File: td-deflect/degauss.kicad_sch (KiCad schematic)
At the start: 10 parts

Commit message: more updates
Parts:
- R108, R109: renamed from R?; footprint (none) -> Resistor_SMD:R_0805_2012Metric_Pad1.15x1.40mm_HandSolder
- gave numbers to parts that had none: 8
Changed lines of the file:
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@@
   (symbol (lib_id "Connector:Conn_01x02_Male") (at 181.61 95.25 0) (mirror y) (unit 1)
     (in_bom yes) (on_board yes) (dnp no)
-    (property "Reference" "J?" (at 178.8668 90.6526 0)
+    (property "Reference" "J15" (at 178.8668 90.6526 0)
       (effects (font (size 1.27 1.27)))
     )
@@
       (project "td-deflect"
         (path "/55a1a5e1-4d11-4c3e-b2b4-b9d50ddc5f9d/76858b88-020a-4ca7-9465-04c6cdf1756c"
-          (reference "J?") (unit 1)
+          (reference "J15") (unit 1)
         )
       )
@@
   (symbol (lib_id "Driver_FET:MCP1416") (at 128.27 83.82 0) (unit 1)
     (in_bom yes) (on_board yes) (dnp no)
-    (property "Reference" "U?" (at 139.5476 82.6516 0)
+    (property "Reference" "U38" (at 139.5476 82.6516 0)
       (effects (font (size 1.27 1.27)) (justify left))
     )
@@
       (project "td-deflect"
         (path "/55a1a5e1-4d11-4c3e-b2b4-b9d50ddc5f9d/76858b88-020a-4ca7-9465-04c6cdf1756c"
-          (reference "U?") (unit 1)
+          (reference "U38") (unit 1)
         )
       )
@@
   (symbol (lib_id "power:+12V") (at 96.52 81.28 0) (unit 1)
     (in_bom yes) (on_board yes) (dnp no)
-    (property "Reference" "#PWR?" (at 96.52 85.09 0)
+    (property "Reference" "#PWR0218" (at 96.52 85.09 0)
       (effects (font (size 1.27 1.27)) hide)
     )
@@
       (project "td-deflect"
         (path "/55a1a5e1-4d11-4c3e-b2b4-b9d50ddc5f9d/76858b88-020a-4ca7-9465-04c6cdf1756c"
-          (reference "#PWR?") (unit 1)
+          (reference "#PWR0218") (unit 1)
         )
       )
@@
   (symbol (lib_id "Transistor_FET:IPD50R380CE") (at 151.13 83.82 0) (unit 1)
     (in_bom yes) (on_board yes) (dnp no)
-    (property "Reference" "Q?" (at 147.32 87.63 0)
+    (property "Reference" "Q22" (at 147.32 87.63 0)
       (effects (font (size 1.27 1.27)) (justify left))
     )
@@
       (project "td-deflect"
         (path "/55a1a5e1-4d11-4c3e-b2b4-b9d50ddc5f9d/76858b88-020a-4ca7-9465-04c6cdf1756c"
-          (reference "Q?") (unit 1)
+          (reference "Q22") (unit 1)
         )
       )
@@
   (symbol (lib_id "power:GND") (at 168.91 88.9 0) (unit 1)
     (in_bom yes) (on_board yes) (dnp no) (fields_autoplaced)
-    (property "Reference" "#PWR?" (at 168.91 95.25 0)
+    (property "Reference" "#PWR0214" (at 168.91 95.25 0)
       (effects (font (size 1.27 1.27)) hide)
     )
@@
       (project "td-deflect"
         (path "/55a1a5e1-4d11-4c3e-b2b4-b9d50ddc5f9d/76858b88-020a-4ca7-9465-04c6cdf1756c"
-          (reference "#PWR?") (unit 1)
+          (reference "#PWR0214") (unit 1)
         )
       )
@@
   (symbol (lib_id "Device:C") (at 96.52 85.09 0) (unit 1)
     (in_bom yes) (on_board yes) (dnp no)
-    (property "Reference" "C?" (at 99.441 83.9216 0)
+    (property "Reference" "C88" (at 99.441 83.9216 0)
       (effects (font (size 1.27 1.27)) (justify left))
     )
@@
       (project "td-deflect"
         (path "/55a1a5e1-4d11-4c3e-b2b4-b9d50ddc5f9d/76858b88-020a-4ca7-9465-04c6cdf1756c"
-          (reference "C?") (unit 1)
+          (reference "C88") (unit 1)
         )
       )
@@
   (symbol (lib_id "power:GND") (at 128.27 91.44 0) (unit 1)
     (in_bom yes) (on_board yes) (dnp no) (fields_autoplaced)
-    (property "Reference" "#PWR?" (at 128.27 97.79 0)
+    (property "Reference" "#PWR0216" (at 128.27 97.79 0)
       (effects (font (size 1.27 1.27)) hide)
     )
@@
       (project "td-deflect"
         (path "/55a1a5e1-4d11-4c3e-b2b4-b9d50ddc5f9d/76858b88-020a-4ca7-9465-04c6cdf1756c"
-          (reference "#PWR?") (unit 1)
+          (reference "#PWR0216") (unit 1)
         )
       )
@@
   (symbol (lib_id "power:+12V") (at 128.27 76.2 0) (unit 1)
     (in_bom yes) (on_board yes) (dnp no) (fields_autoplaced)
-    (property "Reference" "#PWR?" (at 128.27 80.01 0)
+    (property "Reference" "#PWR0217" (at 128.27 80.01 0)
       (effects (font (size 1.27 1.27)) hide)
     )
@@
       (project "td-deflect"
         (path "/55a1a5e1-4d11-4c3e-b2b4-b9d50ddc5f9d/76858b88-020a-4ca7-9465-04c6cdf1756c"
-          (reference "#PWR?") (unit 1)
+          (reference "#PWR0217") (unit 1)
         )
       )
@@
   (symbol (lib_id "power:GND") (at 96.52 88.9 0) (unit 1)
     (in_bom yes) (on_board yes) (dnp no)
-    (property "Reference" "#PWR?" (at 96.52 95.25 0)
+    (property "Reference" "#PWR0219" (at 96.52 95.25 0)
       (effects (font (size 1.27 1.27)) hide)
     )
@@
       (project "td-deflect"
         (path "/55a1a5e1-4d11-4c3e-b2b4-b9d50ddc5f9d/76858b88-020a-4ca7-9465-04c6cdf1756c"
-          (reference "#PWR?") (unit 1)
+          (reference "#PWR0219") (unit 1)
         )
       )
@@
   (symbol (lib_id "power:HT") (at 168.91 57.15 0) (unit 1)
     (in_bom yes) (on_board yes) (dnp no) (fields_autoplaced)
-    (property "Reference" "#PWR?" (at 168.91 54.102 0)
+    (property "Reference" "#PWR0213" (at 168.91 54.102 0)
       (effects (font (size 1.27 1.27)) hide)
     )
@@
       (project "td-deflect"
         (path "/55a1a5e1-4d11-4c3e-b2b4-b9d50ddc5f9d/76858b88-020a-4ca7-9465-04c6cdf1756c"
-          (reference "#PWR?") (unit 1)
+          (reference "#PWR0213") (unit 1)
         )
       )
@@
   (symbol (lib_id "Diode:BA157") (at 168.91 62.23 90) (unit 1)
     (in_bom yes) (on_board yes) (dnp no)
-    (property "Reference" "D?" (at 174.3964 62.23 0)
+    (property "Reference" "D20" (at 174.3964 62.23 0)
       (effects (font (size 1.27 1.27)))
     )
@@
       (project "td-deflect"
         (path "/55a1a5e1-4d11-4c3e-b2b4-b9d50ddc5f9d/76858b88-020a-4ca7-9465-04c6cdf1756c"
-          (reference "D?") (unit 1)
+          (reference "D20") (unit 1)
         )
       )
@@
   (symbol (lib_id "Device:R") (at 116.84 87.63 0) (unit 1)
     (in_bom yes) (on_board yes) (dnp no) (fields_autoplaced)
-    (property "Reference" "R?" (at 119.38 86.3599 0)
+    (property "Reference" "R108" (at 119.38 86.3599 0)
       (effects (font (size 1.27 1.27)) (justify left))
     )
@@
       (effects (font (size 1.27 1.27)) (justify left))
     )
-    (property "Footprint" "" (at 115.062 87.63 90)
+    (property "Footprint" "Resistor_SMD:R_0805_2012Metric_Pad1.15x1.40mm_HandSolder" (at 115.062 87.63 90)
       (effects (font (size 1.27 1.27)) hide)
     )
@@
       (project "td-deflect"
         (path "/55a1a5e1-4d11-4c3e-b2b4-b9d50ddc5f9d/76858b88-020a-4ca7-9465-04c6cdf1756c"
-          (reference "R?") (unit 1)
+          (reference "R108") (unit 1)
         )
       )
@@
   (symbol (lib_id "Device:R") (at 168.91 69.85 0) (unit 1)
     (in_bom yes) (on_board yes) (dnp no) (fields_autoplaced)
-    (property "Reference" "R?" (at 171.45 68.5799 0)
+    (property "Reference" "R110" (at 171.45 68.5799 0)
       (effects (font (size 1.27 1.27)) (justify left))
     )
@@
       (project "td-deflect"
         (path "/55a1a5e1-4d11-4c3e-b2b4-b9d50ddc5f9d/76858b88-020a-4ca7-9465-04c6cdf1756c"
-          (reference "R?") (unit 1)
+          (reference "R110") (unit 1)
         )
       )
@@
   (symbol (lib_id "Device:C") (at 168.91 77.47 0) (unit 1)
     (in_bom yes) (on_board yes) (dnp no)
-    (property "Reference" "C?" (at 171.831 76.3016 0)
+    (property "Reference" "C89" (at 171.831 76.3016 0)
       (effects (font (size 1.27 1.27)) (justify left))
     )
@@
       (project "td-deflect"
         (path "/55a1a5e1-4d11-4c3e-b2b4-b9d50ddc5f9d/76858b88-020a-4ca7-9465-04c6cdf1756c"
-          (reference "C?") (unit 1)
+          (reference "C89") (unit 1)
         )
       )
@@
   (symbol (lib_id "Connector:Conn_01x02_Male") (at 176.53 82.55 0) (mirror y) (unit 1)
     (in_bom yes) (on_board yes) (dnp no)
-    (property "Reference" "J?" (at 173.7868 77.9526 0)
+    (property "Reference" "J12" (at 173.7868 77.9526 0)
       (effects (font (size 1.27 1.27)))
     )
@@
       (project "td-deflect"
         (path "/55a1a5e1-4d11-4c3e-b2b4-b9d50ddc5f9d/76858b88-020a-4ca7-9465-04c6cdf1756c"
-          (reference "J?") (unit 1)
+          (reference "J12") (unit 1)
         )
       )
@@
   (symbol (lib_id "power:GND") (at 116.84 91.44 0) (unit 1)
     (in_bom yes) (on_board yes) (dnp no) (fields_autoplaced)
-    (property "Reference" "#PWR?" (at 116.84 97.79 0)
+    (property "Reference" "#PWR0215" (at 116.84 97.79 0)
       (effects (font (size 1.27 1.27)) hide)
     )
@@
       (project "td-deflect"
         (path "/55a1a5e1-4d11-4c3e-b2b4-b9d50ddc5f9d/76858b88-020a-4ca7-9465-04c6cdf1756c"
-          (reference "#PWR?") (unit 1)
+          (reference "#PWR0215") (unit 1)
         )
       )
@@
   (symbol (lib_id "Device:R") (at 142.24 83.82 90) (unit 1)
     (in_bom yes) (on_board yes) (dnp no) (fields_autoplaced)
-    (property "Reference" "R?" (at 142.24 77.47 90)
+    (property "Reference" "R109" (at 142.24 77.47 90)
       (effects (font (size 1.27 1.27)))
     )
@@
       (effects (font (size 1.27 1.27)))
     )
-    (property "Footprint" "" (at 142.24 85.598 90)
+    (property "Footprint" "Resistor_SMD:R_0805_2012Metric_Pad1.15x1.40mm_HandSolder" (at 142.24 85.598 90)
       (effects (font (size 1.27 1.27)) hide)
     )
@@
       (project "td-deflect"
         (path "/55a1a5e1-4d11-4c3e-b2b4-b9d50ddc5f9d/76858b88-020a-4ca7-9465-04c6cdf1756c"
-          (reference "R?") (unit 1)
-        )
-      )
+          (reference "R109") (unit 1)
+        )
+      )

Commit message: switch to new 0805 footprint
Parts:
- C88: footprint Capacitor_SMD:C_0805_2012Metric_Pad1.15x1.40mm_HandSolder -> Capacitor_SMD:C_0805_2012Metric_Pad1.18x1.45mm_HandSolder
- R108, R109: footprint Resistor_SMD:R_0805_2012Metric_Pad1.15x1.40mm_HandSolder -> Resistor_SMD:R_0805_2012Metric_Pad1.20x1.40mm_HandSolder
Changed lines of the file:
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@@
       (effects (font (size 1.27 1.27)) (justify left))
     )
-    (property "Footprint" "Capacitor_SMD:C_0805_2012Metric_Pad1.15x1.40mm_HandSolder" (at 97.4852 88.9 0)
+    (property "Footprint" "Capacitor_SMD:C_0805_2012Metric_Pad1.18x1.45mm_HandSolder" (at 97.4852 88.9 0)
       (effects (font (size 1.27 1.27)) hide)
     )
@@
       (effects (font (size 1.27 1.27)) (justify left))
     )
-    (property "Footprint" "Resistor_SMD:R_0805_2012Metric_Pad1.15x1.40mm_HandSolder" (at 115.062 87.63 90)
+    (property "Footprint" "Resistor_SMD:R_0805_2012Metric_Pad1.20x1.40mm_HandSolder" (at 115.062 87.63 90)
       (effects (font (size 1.27 1.27)) hide)
     )
@@
       (effects (font (size 1.27 1.27)))
     )
-    (property "Footprint" "Resistor_SMD:R_0805_2012Metric_Pad1.15x1.40mm_HandSolder" (at 142.24 85.598 90)
-      (effects (font (size 1.27 1.27)) hide)
-    )
+    (property "Footprint" "Resistor_SMD:R_0805_2012Metric_Pad1.20x1.40mm_HandSolder" (at 142.24 85.598 90)
+      (effects (font (size 1.27 1.27)) hide)
+    )

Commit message: fix drc errors
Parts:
- J12, J15: symbol Connector:Conn_01x02_Male -> Connector:Conn_01x02_Pin
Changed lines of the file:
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@@
     )
   )
-  (symbol (lib_id "Connector:Conn_01x02_Male") (at 181.61 95.25 0) (mirror y) (unit 1)
+  (symbol (lib_id "Connector:Conn_01x02_Pin") (at 181.61 95.25 0) (mirror y) (unit 1)
     (in_bom yes) (on_board yes) (dnp no)
     (property "Reference" "J15" (at 178.8668 90.6526 0)
@@
     )
   )
-  (symbol (lib_id "Connector:Conn_01x02_Male") (at 176.53 82.55 0) (mirror y) (unit 1)
+  (symbol (lib_id "Connector:Conn_01x02_Pin") (at 176.53 82.55 0) (mirror y) (unit 1)
     (in_bom yes) (on_board yes) (dnp no)
     (property "Reference" "J12" (at 173.7868 77.9526 0)

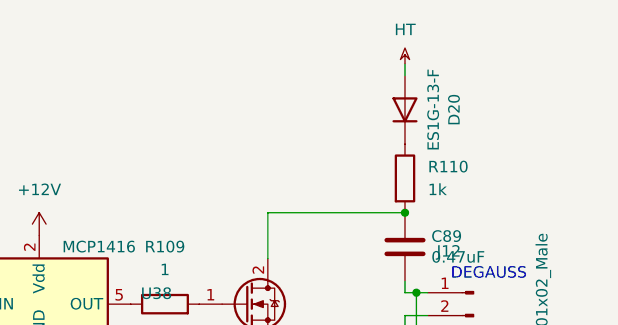
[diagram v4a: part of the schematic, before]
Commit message: fix remaining erc errors
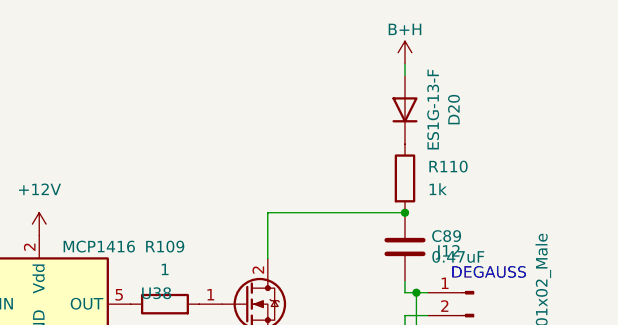
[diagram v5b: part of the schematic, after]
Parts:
- D20: footprint Diode_SMD:D_SMA -> Diode_THT:D_DO-41_SOD81_P10.16mm_Horizontal
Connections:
- net HT renamed B+H
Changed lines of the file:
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@@
+    )
+  )
+  (symbol (lib_id "td-crt:B+H") (at 168.91 57.15 0) (unit 1)
+    (in_bom yes) (on_board yes) (dnp no) (fields_autoplaced)
+    (property "Reference" "#PWR024" (at 168.91 60.96 0)
+      (effects (font (size 1.27 1.27)) hide)
+    )
+    (property "Value" "B+H" (at 168.91 53.34 0)
+      (effects (font (size 1.27 1.27)))
+    )
+    (property "Footprint" "" (at 168.91 57.15 0)
+      (effects (font (size 1.27 1.27)) hide)
+    )
+    (property "Datasheet" "" (at 168.91 57.15 0)
+      (effects (font (size 1.27 1.27)) hide)
+    )
+    (pin "1")
+    (instances
+      (project "td-deflect"
+        (path "/55a1a5e1-4d11-4c3e-b2b4-b9d50ddc5f9d/76858b88-020a-4ca7-9465-04c6cdf1756c"
+          (reference "#PWR024") (unit 1)
+        )
+      )
     )
   )
@@
     )
   )
-  (symbol (lib_id "power:HT") (at 168.91 57.15 0) (unit 1)
-    (in_bom yes) (on_board yes) (dnp no) (fields_autoplaced)
-    (property "Reference" "#PWR0213" (at 168.91 54.102 0)
-      (effects (font (size 1.27 1.27)) hide)
-    )
-    (property "Value" "HT" (at 168.91 53.34 0)
-      (effects (font (size 1.27 1.27)))
-    )
-    (property "Footprint" "" (at 168.91 57.15 0)
-      (effects (font (size 1.27 1.27)) hide)
-    )
-    (property "Datasheet" "" (at 168.91 57.15 0)
-      (effects (font (size 1.27 1.27)) hide)
-    )
-    (pin "1")
-    (instances
-      (project "td-deflect"
-        (path "/55a1a5e1-4d11-4c3e-b2b4-b9d50ddc5f9d/76858b88-020a-4ca7-9465-04c6cdf1756c"
-          (reference "#PWR0213") (unit 1)
-        )
-      )
-    )
-  )
   (symbol (lib_id "Diode:BA157") (at 168.91 62.23 90) (unit 1)
     (in_bom yes) (on_board yes) (dnp no)
@@
       (effects (font (size 1.27 1.27)))
     )
-    (property "Footprint" "Diode_SMD:D_SMA" (at 173.355 62.23 0)
-      (effects (font (size 1.27 1.27)) hide)
-    )
-    (property "Datasheet" "" (at 168.91 62.23 0)
-      (effects (font (size 1.27 1.27)) hide)
-    )
+    (property "Footprint" "Diode_THT:D_DO-41_SOD81_P10.16mm_Horizontal" (at 173.355 62.23 0)
+      (effects (font (size 1.27 1.27)) hide)
+    )
+    (property "Datasheet" "https://www.vishay.com/docs/88536/ba157.pdf" (at 168.91 62.23 0)
+      (effects (font (size 1.27 1.27)) hide)
+    )

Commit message: more layout work
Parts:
- removed J15: Conn_01x02_Male, td-deflect:monitor_10_8_2p, symbol Connector:Conn_01x02_Pin
- D20: footprint Diode_THT:D_DO-41_SOD81_P10.16mm_Horizontal -> Diode_SMD:D_SMA
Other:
- note removed: "DEGAUSS 2"
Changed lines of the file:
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@@
 (kicad_sch (version 20230121) (generator eeschema)
   (paper "A4")
-  (junction (at 170.18 82.55) (diameter 0) (color 0 0 0 0)
-  )
   (junction (at 116.84 83.82) (diameter 0) (color 0 0 0 0)
   )
@@
   (junction (at 168.91 73.66) (diameter 0) (color 0 0 0 0)
   )
-  (wire (pts (xy 170.18 87.63) (xy 176.53 87.63))
-    (stroke (width 0) (type default))
-  )
   (wire (pts (xy 168.91 85.09) (xy 168.91 88.9))
     (stroke (width 0) (type default))
   )
-  (wire (pts (xy 170.18 82.55) (xy 171.45 82.55))
-    (stroke (width 0) (type default))
-  )
   (wire (pts (xy 168.91 57.15) (xy 168.91 58.42))
     (stroke (width 0) (type default))
@@
     (stroke (width 0) (type default))
   )
-  (wire (pts (xy 171.45 97.79) (xy 176.53 97.79))
-    (stroke (width 0) (type default))
-  )
   (wire (pts (xy 168.91 81.28) (xy 168.91 82.55))
     (stroke (width 0) (type default))
   )
-  (wire (pts (xy 168.91 82.55) (xy 170.18 82.55))
+  (wire (pts (xy 168.91 82.55) (xy 171.45 82.55))
     (stroke (width 0) (type default))
   )
@@
     (stroke (width 0) (type default))
   )
-  (wire (pts (xy 171.45 88.9) (xy 171.45 97.79))
-    (stroke (width 0) (type default))
-  )
   (wire (pts (xy 171.45 85.09) (xy 168.91 85.09))
     (stroke (width 0) (type default))
   )
-  (wire (pts (xy 176.53 87.63) (xy 176.53 95.25))
-    (stroke (width 0) (type default))
-  )
-  (wire (pts (xy 170.18 82.55) (xy 170.18 87.63))
-    (stroke (width 0) (type default))
-  )
-  (wire (pts (xy 168.91 88.9) (xy 171.45 88.9))
-    (stroke (width 0) (type default))
-  )
   (wire (pts (xy 116.84 83.82) (xy 120.65 83.82))
     (stroke (width 0) (type default))
-  )
-  (text "DEGAUSS 2" (at 173.99 100.33 0)
-    (effects (font (size 1.27 1.27)) (justify left bottom))
   )
   (text "DEGAUSS" (at 173.99 81.28 0)
@@
     )
   )
-  (symbol (lib_id "Connector:Conn_01x02_Pin") (at 181.61 95.25 0) (mirror y) (unit 1)
-    (in_bom yes) (on_board yes) (dnp no)
-    (property "Reference" "J15" (at 178.8668 90.6526 0)
-      (effects (font (size 1.27 1.27)))
-    )
-    (property "Value" "Conn_01x02_Male" (at 189.23 96.52 90)
-      (effects (font (size 1.27 1.27)))
-    )
-    (property "Footprint" "td-deflect:monitor_10_8_2p" (at 181.61 95.25 0)
-      (effects (font (size 1.27 1.27)) hide)
-    )
-    (property "Datasheet" "~" (at 181.61 95.25 0)
-      (effects (font (size 1.27 1.27)) hide)
-    )
-    (pin "1")
-    (pin "2")
-    (instances
-      (project "td-deflect"
-        (path "/55a1a5e1-4d11-4c3e-b2b4-b9d50ddc5f9d/76858b88-020a-4ca7-9465-04c6cdf1756c"
-          (reference "J15") (unit 1)
-        )
-      )
-    )
-  )
   (symbol (lib_id "Driver_FET:MCP1416") (at 128.27 83.82 0) (unit 1)
     (in_bom yes) (on_board yes) (dnp no)
@@
       (effects (font (size 1.27 1.27)))
     )
-    (property "Footprint" "Diode_THT:D_DO-41_SOD81_P10.16mm_Horizontal" (at 173.355 62.23 0)
-      (effects (font (size 1.27 1.27)) hide)
-    )
+    (property "Footprint" "Diode_SMD:D_SMA" (at 173.355 62.23 0)
+      (effects (font (size 1.27 1.27)) hide)
+    )

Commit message: update pcb
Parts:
- C88: Digikey 1276-1099-1-ND -> 311-1140-1-ND
- J12: Digikey (none) -> DNP
- R108, R109: Digikey (none) -> 311-1.00CRCT-ND
- R110: footprint Resistor_THT:R_Radial_Power_L11.0mm_W7.0mm_P5.00mm -> Resistor_THT:R_Radial_Power_L13.0mm_W9.0mm_P5.00mm; Digikey (none) -> TWM5J1K0E-ND
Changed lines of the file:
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@@
       (effects (font (size 1.27 1.27)) hide)
     )
-    (property "Digikey" "1276-1099-1-ND" (at 96.52 85.09 0)
+    (property "Digikey" "311-1140-1-ND" (at 96.52 85.09 0)
       (effects (font (size 1.27 1.27)) hide)
     )
@@
       (effects (font (size 1.27 1.27)) hide)
     )
+    (property "Digikey" "311-1.00CRCT-ND" (at 116.84 87.63 0)
+      (effects (font (size 1.27 1.27)) hide)
+    )
     (pin "1")
     (pin "2")
@@
       (effects (font (size 1.27 1.27)) (justify left))
     )
-    (property "Footprint" "Resistor_THT:R_Radial_Power_L11.0mm_W7.0mm_P5.00mm" (at 167.132 69.85 90)
+    (property "Footprint" "Resistor_THT:R_Radial_Power_L13.0mm_W9.0mm_P5.00mm" (at 167.132 69.85 90)
       (effects (font (size 1.27 1.27)) hide)
     )
@@
       (effects (font (size 1.27 1.27)) hide)
     )
+    (property "Digikey" "TWM5J1K0E-ND" (at 168.91 69.85 0)
+      (effects (font (size 1.27 1.27)) hide)
+    )
     (pin "1")
     (pin "2")
@@
       (effects (font (size 1.27 1.27)) hide)
     )
+    (property "Digikey" "DNP" (at 176.53 82.55 0)
+      (effects (font (size 1.27 1.27)) hide)
+    )
     (pin "1")
     (pin "2")
@@
       (effects (font (size 1.27 1.27)) hide)
     )
+    (property "Digikey" " 311-1.00CRCT-ND" (at 142.24 83.82 0)
+      (effects (font (size 1.27 1.27)) hide)
+    )
